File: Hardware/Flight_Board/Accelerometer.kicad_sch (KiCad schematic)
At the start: 4 parts

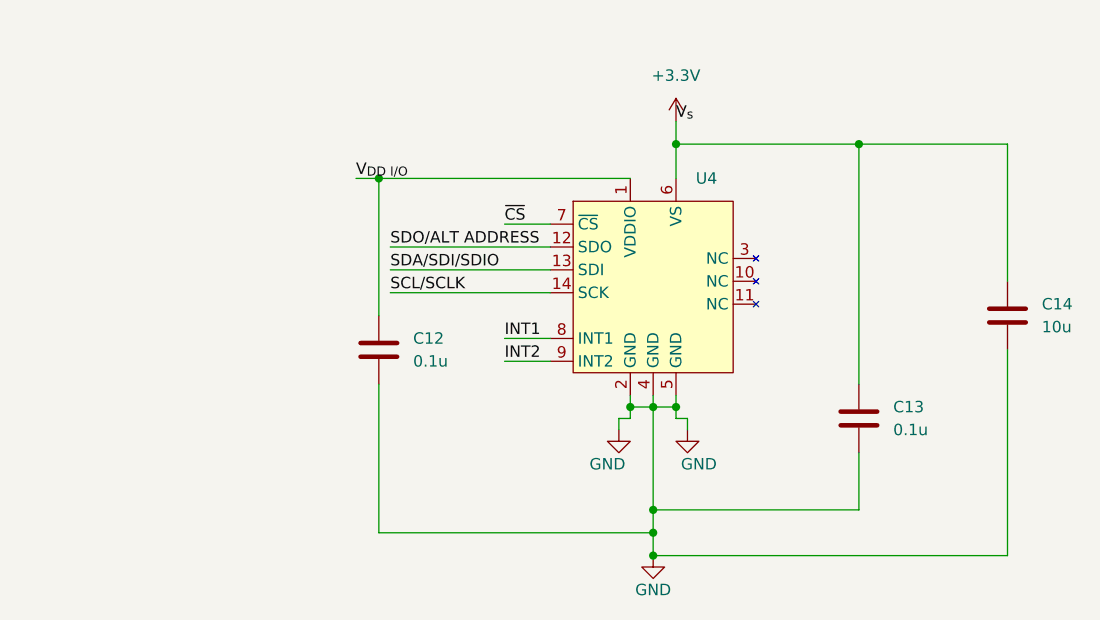
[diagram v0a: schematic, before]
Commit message: standardize connections and create initial spi2 bus
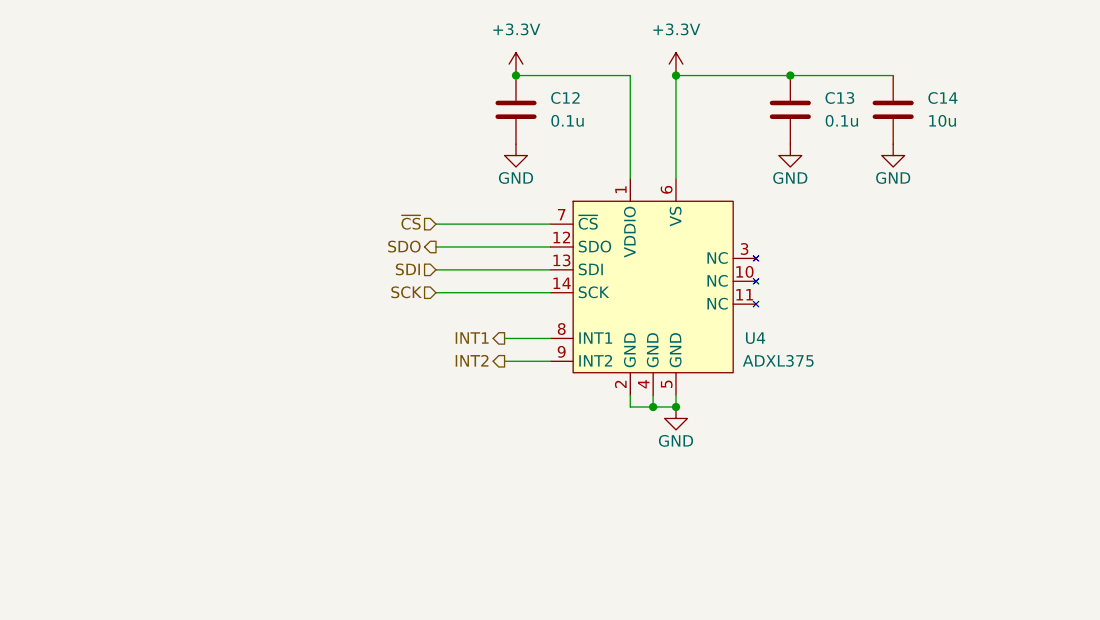
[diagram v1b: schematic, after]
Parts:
- U4: value ~ -> ADXL375
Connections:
- net +3.3V: now also C12.2, U4.1 (VDDIO)
- net GND: now also C12.1; no longer C12.2
- net SCL/SCLK renamed SCK
- net SDA/SDI/SDIO renamed SDI
- net SDO/ALT ADDRESS renamed SDO
- removed net V_{DD I/O}: C12.1, U4.1 (VDDIO)
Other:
- moved on the sheet: C12, C13, C14

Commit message: move ADLX375 to I2C, bring out more mcu pins, and general touchups
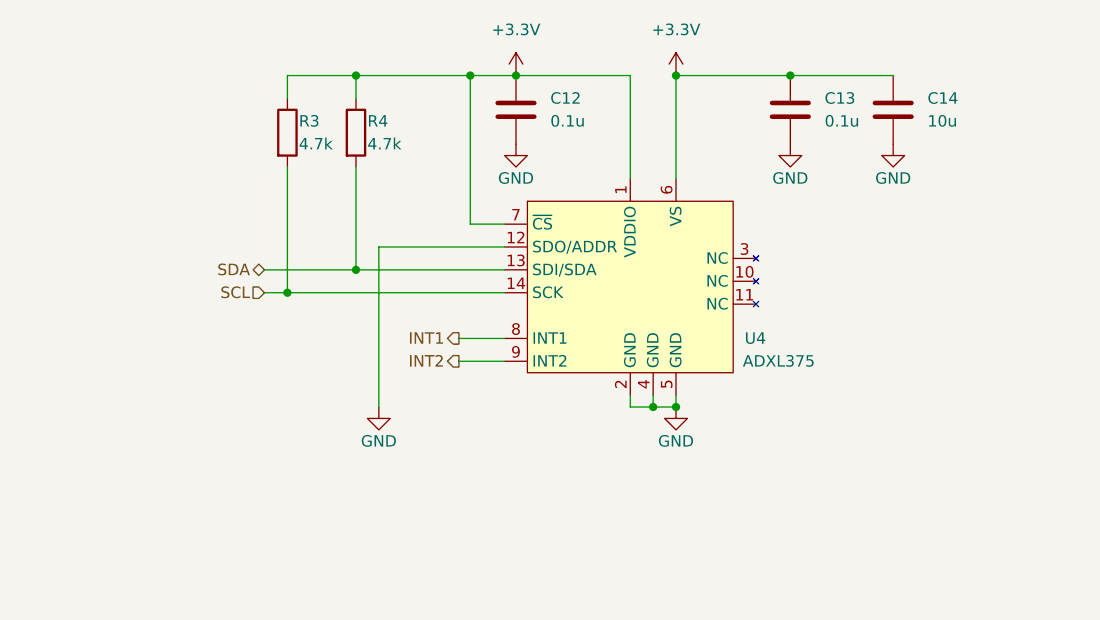
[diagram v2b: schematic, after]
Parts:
- added R3, R4: 4.7k, symbol Device:R
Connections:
- net SDO is gone; now on net GND: U4.12 (SDO/ADDR)
- net ~{CS} is gone; now on net +3.3V: U4.7 (~{CS})
- net +3.3V: now also R3.1, R4.1
- net SCK renamed SCL
- net SCL: now also R3.2
- net SDI renamed SDA
- net SDA: now also R4.2
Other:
- moved on the sheet: U4
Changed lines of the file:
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@@
   (junction (at 179.07 55.88) (diameter 0) (color 0 0 0 0)
   )
+  (junction (at 143.51 55.88) (diameter 0) (color 0 0 0 0)
+  )
+  (junction (at 143.51 77.47) (diameter 0) (color 0 0 0 0)
+  )
   (junction (at 179.07 92.71) (diameter 0) (color 0 0 0 0)
   )
   (junction (at 191.77 55.88) (diameter 0) (color 0 0 0 0)
   )
+  (junction (at 156.21 55.88) (diameter 0) (color 0 0 0 0)
+  )
   (junction (at 161.29 55.88) (diameter 0) (color 0 0 0 0)
   )
+  (junction (at 135.89 80.01) (diameter 0) (color 0 0 0 0)
+  )
   (junction (at 176.53 92.71) (diameter 0) (color 0 0 0 0)
   )
-  (wire (pts (xy 152.4 80.01) (xy 165.1 80.01))
-    (stroke (width 0) (type default))
-  )
-  (wire (pts (xy 152.4 72.39) (xy 165.1 72.39))
+  (wire (pts (xy 160.02 72.39) (xy 156.21 72.39))
+    (stroke (width 0) (type default))
+  )
+  (wire (pts (xy 133.35 80.01) (xy 135.89 80.01))
+    (stroke (width 0) (type default))
+  )
+  (wire (pts (xy 143.51 77.47) (xy 160.02 77.47))
     (stroke (width 0) (type default))
   )
@@
     (stroke (width 0) (type default))
   )
+  (wire (pts (xy 135.89 66.04) (xy 135.89 80.01))
+    (stroke (width 0) (type default))
+  )
+  (wire (pts (xy 135.89 55.88) (xy 135.89 58.42))
+    (stroke (width 0) (type default))
+  )
   (wire (pts (xy 191.77 55.88) (xy 179.07 55.88))
     (stroke (width 0) (type default))
@@
     (stroke (width 0) (type default))
   )
+  (wire (pts (xy 160.02 74.93) (xy 146.05 74.93))
+    (stroke (width 0) (type default))
+  )
   (wire (pts (xy 179.07 92.71) (xy 176.53 92.71))
     (stroke (width 0) (type default))
   )
-  (wire (pts (xy 160.02 87.63) (xy 165.1 87.63))
-    (stroke (width 0) (type default))
-  )
-  (wire (pts (xy 152.4 74.93) (xy 165.1 74.93))
-    (stroke (width 0) (type default))
-  )
-  (wire (pts (xy 160.02 85.09) (xy 165.1 85.09))
+  (wire (pts (xy 154.94 87.63) (xy 160.02 87.63))
+    (stroke (width 0) (type default))
+  )
+  (wire (pts (xy 143.51 55.88) (xy 135.89 55.88))
+    (stroke (width 0) (type default))
+  )
+  (wire (pts (xy 146.05 74.93) (xy 146.05 92.71))
+    (stroke (width 0) (type default))
+  )
+  (wire (pts (xy 154.94 85.09) (xy 160.02 85.09))
     (stroke (width 0) (type default))
   )
@@
     (stroke (width 0) (type default))
   )
+  (wire (pts (xy 143.51 55.88) (xy 143.51 58.42))
+    (stroke (width 0) (type default))
+  )
   (wire (pts (xy 173.99 91.44) (xy 173.99 92.71))
     (stroke (width 0) (type default))
@@
     (stroke (width 0) (type default))
   )
+  (wire (pts (xy 135.89 80.01) (xy 160.02 80.01))
+    (stroke (width 0) (type default))
+  )
+  (wire (pts (xy 156.21 72.39) (xy 156.21 55.88))
+    (stroke (width 0) (type default))
+  )
   (wire (pts (xy 179.07 92.71) (xy 179.07 91.44))
     (stroke (width 0) (type default))
   )
+  (wire (pts (xy 143.51 66.04) (xy 143.51 77.47))
+    (stroke (width 0) (type default))
+  )
   (wire (pts (xy 176.53 91.44) (xy 176.53 92.71))
     (stroke (width 0) (type default))
   )
-  (wire (pts (xy 152.4 77.47) (xy 165.1 77.47))
+  (wire (pts (xy 156.21 55.88) (xy 161.29 55.88))
+    (stroke (width 0) (type default))
+  )
+  (wire (pts (xy 133.35 77.47) (xy 143.51 77.47))
+    (stroke (width 0) (type default))
+  )
+  (wire (pts (xy 143.51 55.88) (xy 156.21 55.88))
     (stroke (width 0) (type default))
   )
@@
     (stroke (width 0) (type default))
   )
-  (hierarchical_label "SDI" (shape input) (at 152.4 77.47 180) (fields_autoplaced)
+  (hierarchical_label "SDA" (shape bidirectional) (at 133.35 77.47 180) (fields_autoplaced)
     (effects (font (size 1.27 1.27)) (justify right))
   )
-  (hierarchical_label "INT1" (shape output) (at 160.02 85.09 180) (fields_autoplaced)
+  (hierarchical_label "INT1" (shape output) (at 154.94 85.09 180) (fields_autoplaced)
     (effects (font (size 1.27 1.27)) (justify right))
   )
-  (hierarchical_label "INT2" (shape output) (at 160.02 87.63 180) (fields_autoplaced)
+  (hierarchical_label "INT2" (shape output) (at 154.94 87.63 180) (fields_autoplaced)
     (effects (font (size 1.27 1.27)) (justify right))
   )
-  (hierarchical_label "~{CS}" (shape input) (at 152.4 72.39 180) (fields_autoplaced)
-    (effects (font (size 1.27 1.27)) (justify right))
-  )
-  (hierarchical_label "SCK" (shape input) (at 152.4 80.01 180) (fields_autoplaced)
-    (effects (font (size 1.27 1.27)) (justify right))
-  )
-  (hierarchical_label "SDO" (shape output) (at 152.4 74.93 180) (fields_autoplaced)
+  (hierarchical_label "SCL" (shape input) (at 133.35 80.01 180) (fields_autoplaced)
     (effects (font (size 1.27 1.27)) (justify right))
   )
@@
     )
   )
+  (symbol (lib_id "Device:R") (at 143.51 62.23 0) (unit 1)
+    (in_bom yes) (on_board yes) (dnp no)
+    (property "Reference" "R4" (at 144.78 60.96 0)
+      (effects (font (size 1.27 1.27)) (justify left))
+    )
+    (property "Value" "4.7k" (at 144.78 63.5 0)
+      (effects (font (size 1.27 1.27)) (justify left))
+    )
+    (property "Footprint" "" (at 141.732 62.23 90)
+      (effects (font (size 1.27 1.27)) hide)
+    )
+    (property "Datasheet" "~" (at 143.51 62.23 0)
+      (effects (font (size 1.27 1.27)) hide)
+    )
+    (pin "1")
+    (pin "2")
+    (instances
+      (project "Flight_Board"
+        (path "/e8eb85d5-f1ff-4500-895d-25b9ff5f6d36/43c0adf1-436b-4b66-9010-44cf9a79cc96"
+          (reference "R4") (unit 1)
+        )
+      )
+    )
+  )
+  (symbol (lib_id "power:GND") (at 146.05 92.71 0) (unit 1)
+    (in_bom yes) (on_board yes) (dnp no)
+    (property "Reference" "#PWR034" (at 146.05 99.06 0)
+      (effects (font (size 1.27 1.27)) hide)
+    )
+    (property "Value" "GND" (at 146.05 96.52 0)
+      (effects (font (size 1.27 1.27)))
+    )
+    (property "Footprint" "" (at 146.05 92.71 0)
+      (effects (font (size 1.27 1.27)) hide)
+    )
+    (property "Datasheet" "" (at 146.05 92.71 0)
+      (effects (font (size 1.27 1.27)) hide)
+    )
+    (pin "1")
+    (instances
+      (project "Flight_Board"
+        (path "/e8eb85d5-f1ff-4500-895d-25b9ff5f6d36/43c0adf1-436b-4b66-9010-44cf9a79cc96"
+          (reference "#PWR034") (unit 1)
+        )
+      )
+    )
+  )
   (symbol (lib_id "Device:C") (at 161.29 59.69 180) (unit 1)
     (in_bom yes) (on_board yes) (dnp no) (fields_autoplaced)
@@
         )
       )
+    )
+  )
+  (symbol (lib_id "Device:R") (at 135.89 62.23 0) (unit 1)
+    (in_bom yes) (on_board yes) (dnp no)
+    (property "Reference" "R3" (at 137.16 60.96 0)
+      (effects (font (size 1.27 1.27)) (justify left))
+    )
+    (property "Value" "4.7k" (at 137.16 63.5 0)
+      (effects (font (size 1.27 1.27)) (justify left))
+    )
+    (property "Footprint" "" (at 134.112 62.23 90)
+      (effects (font (size 1.27 1.27)) hide)
+    )
+    (property "Datasheet" "~" (at 135.89 62.23 0)
+      (effects (font (size 1.27 1.27)) hide)
+    )
+    (pin "1")
+    (pin "2")
+    (instances
+      (project "Flight_Board"
+        (path "/e8eb85d5-f1ff-4500-895d-25b9ff5f6d36/43c0adf1-436b-4b66-9010-44cf9a79cc96"
+          (reference "R3") (unit 1)
+        )
+      )

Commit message: clean up and finalize initial design
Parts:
- renumbered R3 to R2, R4 to R3, U4 to U3
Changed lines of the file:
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@@
   (symbol (lib_id "Project:ADXL375") (at 176.53 78.74 0) (unit 1)
     (in_bom yes) (on_board yes) (dnp no)
-    (property "Reference" "U4" (at 186.69 85.09 0)
+    (property "Reference" "U3" (at 186.69 85.09 0)
       (effects (font (size 1.27 1.27)) (justify left))
     )
@@
       (project "Flight_Board"
         (path "/e8eb85d5-f1ff-4500-895d-25b9ff5f6d36/43c0adf1-436b-4b66-9010-44cf9a79cc96"
-          (reference "U4") (unit 1)
+          (reference "U3") (unit 1)
         )
       )
@@
   (symbol (lib_id "Device:R") (at 143.51 62.23 0) (unit 1)
     (in_bom yes) (on_board yes) (dnp no)
-    (property "Reference" "R4" (at 144.78 60.96 0)
+    (property "Reference" "R3" (at 144.78 60.96 0)
       (effects (font (size 1.27 1.27)) (justify left))
     )
@@
       (project "Flight_Board"
         (path "/e8eb85d5-f1ff-4500-895d-25b9ff5f6d36/43c0adf1-436b-4b66-9010-44cf9a79cc96"
-          (reference "R4") (unit 1)
+          (reference "R3") (unit 1)
         )
       )
@@
   (symbol (lib_id "power:GND") (at 146.05 92.71 0) (unit 1)
     (in_bom yes) (on_board yes) (dnp no)
-    (property "Reference" "#PWR034" (at 146.05 99.06 0)
+    (property "Reference" "#PWR019" (at 146.05 99.06 0)
       (effects (font (size 1.27 1.27)) hide)
     )
@@
       (project "Flight_Board"
         (path "/e8eb85d5-f1ff-4500-895d-25b9ff5f6d36/43c0adf1-436b-4b66-9010-44cf9a79cc96"
-          (reference "#PWR034") (unit 1)
+          (reference "#PWR019") (unit 1)
         )
       )
@@
   (symbol (lib_id "power:GND") (at 203.2 63.5 0) (unit 1)
     (in_bom yes) (on_board yes) (dnp no)
-    (property "Reference" "#PWR019" (at 203.2 69.85 0)
+    (property "Reference" "#PWR025" (at 203.2 69.85 0)
       (effects (font (size 1.27 1.27)) hide)
     )
@@
       (project "Flight_Board"
         (path "/e8eb85d5-f1ff-4500-895d-25b9ff5f6d36/43c0adf1-436b-4b66-9010-44cf9a79cc96"
-          (reference "#PWR019") (unit 1)
+          (reference "#PWR025") (unit 1)
         )
       )
@@
   (symbol (lib_id "power:GND") (at 191.77 63.5 0) (unit 1)
     (in_bom yes) (on_board yes) (dnp no)
-    (property "Reference" "#PWR018" (at 191.77 69.85 0)
+    (property "Reference" "#PWR024" (at 191.77 69.85 0)
       (effects (font (size 1.27 1.27)) hide)
     )
@@
       (project "Flight_Board"
         (path "/e8eb85d5-f1ff-4500-895d-25b9ff5f6d36/43c0adf1-436b-4b66-9010-44cf9a79cc96"
-          (reference "#PWR018") (unit 1)
+          (reference "#PWR024") (unit 1)
         )
       )
@@
   (symbol (lib_id "power:+3.3V") (at 179.07 55.88 0) (unit 1)
     (in_bom yes) (on_board yes) (dnp no) (fields_autoplaced)
-    (property "Reference" "#PWR016" (at 179.07 59.69 0)
+    (property "Reference" "#PWR022" (at 179.07 59.69 0)
       (effects (font (size 1.27 1.27)) hide)
     )
@@
       (project "Flight_Board"
         (path "/e8eb85d5-f1ff-4500-895d-25b9ff5f6d36/43c0adf1-436b-4b66-9010-44cf9a79cc96"
-          (reference "#PWR016") (unit 1)
+          (reference "#PWR022") (unit 1)
         )
       )
@@
   (symbol (lib_id "Device:R") (at 135.89 62.23 0) (unit 1)
     (in_bom yes) (on_board yes) (dnp no)
-    (property "Reference" "R3" (at 137.16 60.96 0)
+    (property "Reference" "R2" (at 137.16 60.96 0)
       (effects (font (size 1.27 1.27)) (justify left))
     )
@@
       (project "Flight_Board"
         (path "/e8eb85d5-f1ff-4500-895d-25b9ff5f6d36/43c0adf1-436b-4b66-9010-44cf9a79cc96"
-          (reference "R3") (unit 1)
+          (reference "R2") (unit 1)
         )
       )
@@
   (symbol (lib_id "power:GND") (at 179.07 92.71 0) (unit 1)
     (in_bom yes) (on_board yes) (dnp no)
-    (property "Reference" "#PWR017" (at 179.07 99.06 0)
+    (property "Reference" "#PWR023" (at 179.07 99.06 0)
       (effects (font (size 1.27 1.27)) hide)
     )
@@
       (project "Flight_Board"
         (path "/e8eb85d5-f1ff-4500-895d-25b9ff5f6d36/43c0adf1-436b-4b66-9010-44cf9a79cc96"
-          (reference "#PWR017") (unit 1)
-        )
-      )
+          (reference "#PWR023") (unit 1)
+        )
+      )

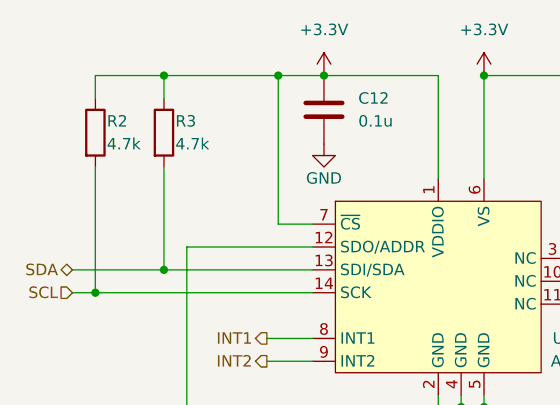
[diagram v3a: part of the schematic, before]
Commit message: Clean up, relabel all refdes, and add autosaved files to gitignore
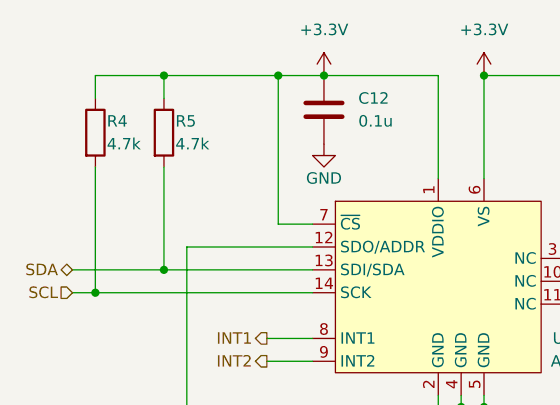
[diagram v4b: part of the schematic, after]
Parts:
- renumbered R2 to R4, R3 to R5

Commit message: clean up, implement suggestions from saunders
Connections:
- net INT2: no longer names the net of U3.9 (INT2)
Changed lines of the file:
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@@
-    (stroke (width 0) (type default))
-  )
-  (wire (pts (xy 154.94 87.63) (xy 160.02 87.63))
     (stroke (width 0) (type default))
   )
@@
     (effects (font (size 1.27 1.27)) (justify right))
   )
-  (hierarchical_label "INT2" (shape output) (at 154.94 87.63 180) (fields_autoplaced)
-    (effects (font (size 1.27 1.27)) (justify right))
-  )
